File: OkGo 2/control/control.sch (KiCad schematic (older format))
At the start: 49 parts, among them P101 BATT, P102 BATT, P103 BATT_CASE, P104 KEYSW, P105 KEYSW, P110 SMA, SW101 LATCHING PUSH, SW102 KEYSWITCH, U101 FUSE 1A, U102 ADP3335, U103 BEZEL, U104 LCD_HD44780, U105 STM32F071CBT6, U106 RFM95W, U107 MEU1S0303ZC, U108 SWD, Y101 8MHz

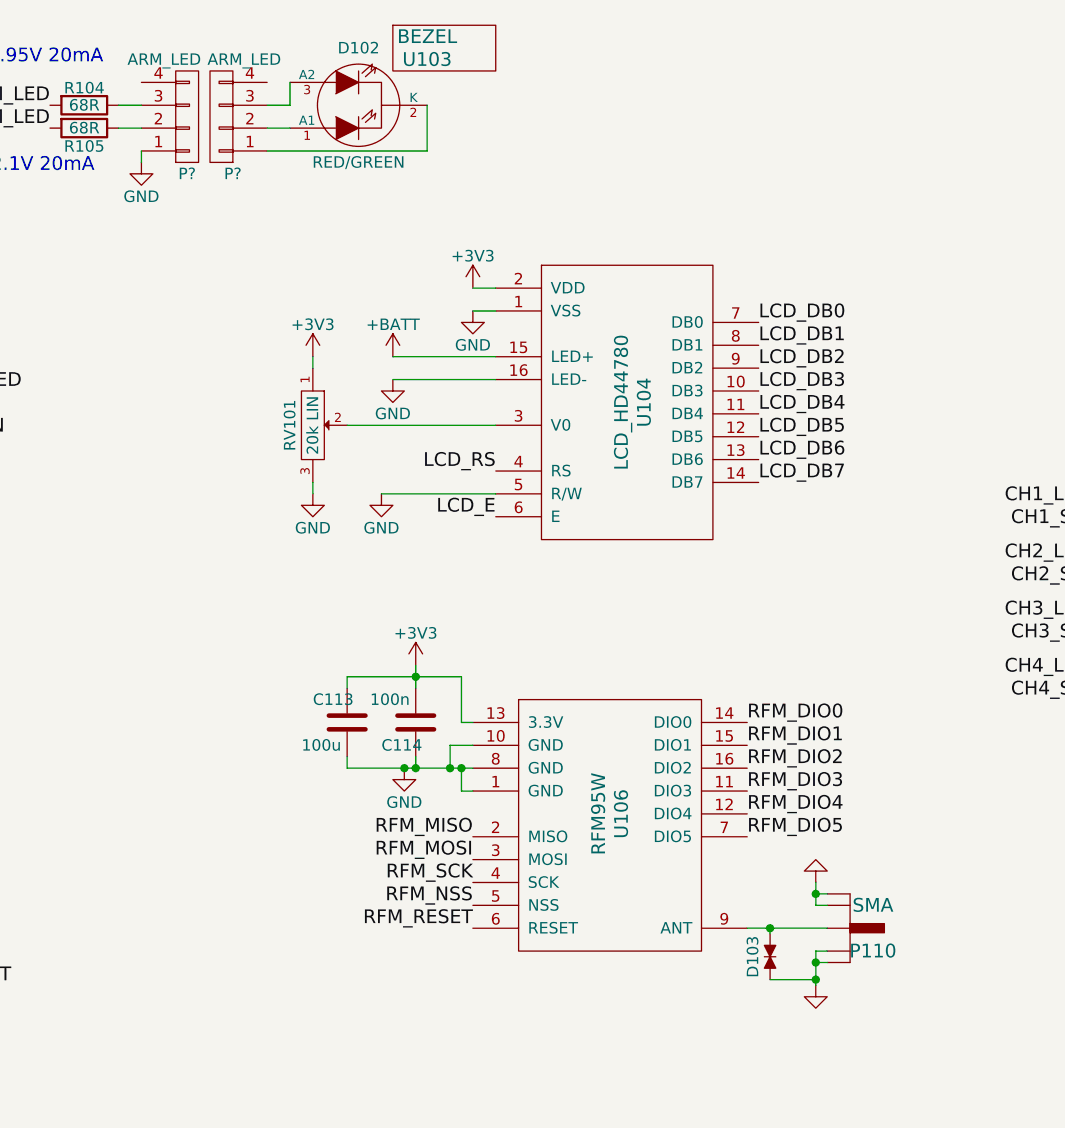
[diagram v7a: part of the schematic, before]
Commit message: Non-handsoldering footprints, fixes #17
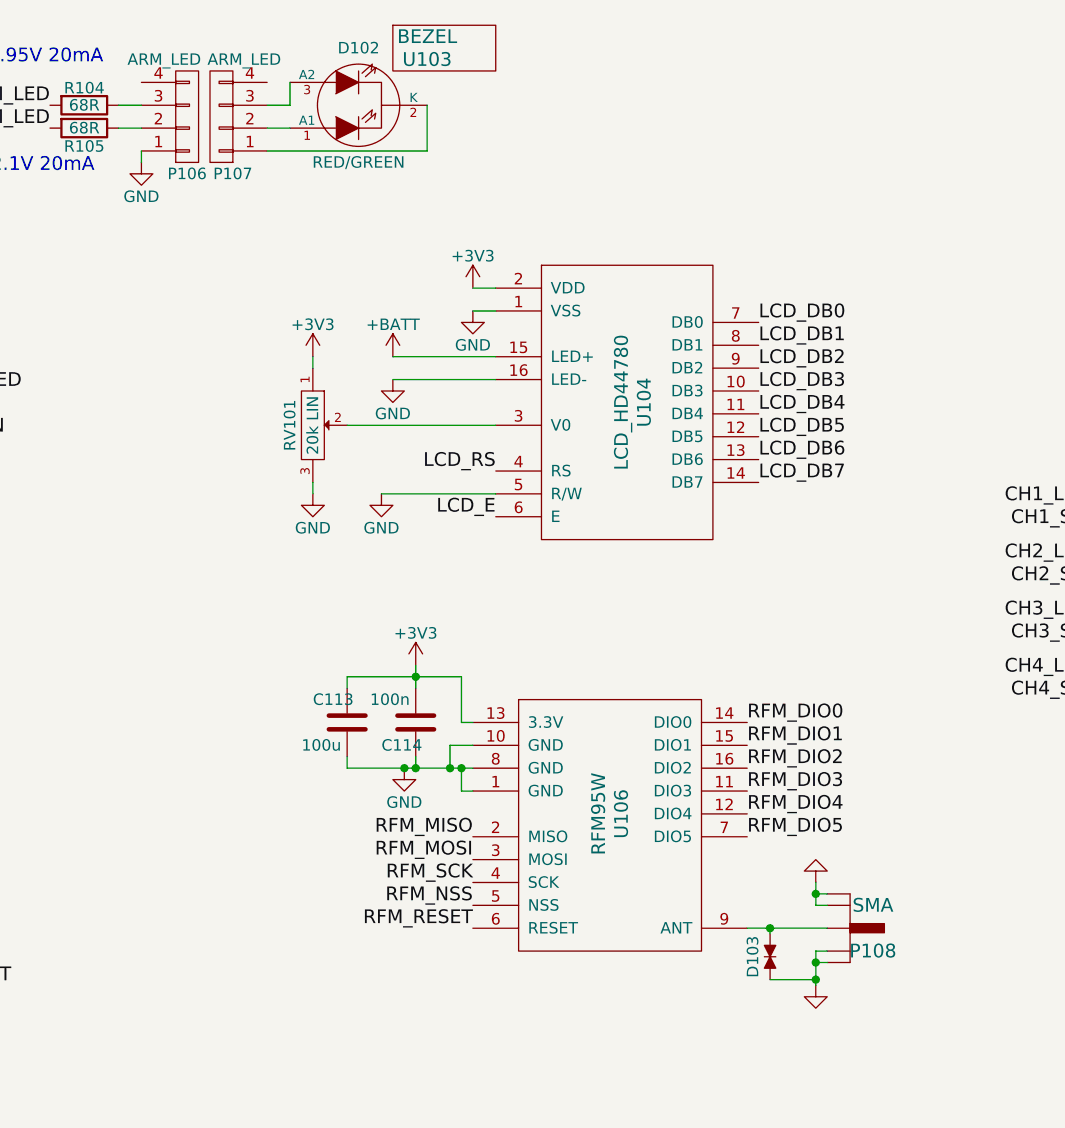
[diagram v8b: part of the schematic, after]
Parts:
- C101, C102, C103, C104, C105, C106, C107, C108, C109, C110, C111, C112, C114, R103: footprint Capacitors_SMD:C_0805_HandSoldering -> Capacitors_SMD:C_0805
- C113: footprint Capacitors_SMD:C_1206_HandSoldering -> Capacitors_SMD:C_1206
- D101, D103: footprint Resistors_SMD:R_0603_HandSoldering -> Resistors_SMD:R_0603
- R101, R102, R104, R105, R106: footprint Resistors_SMD:R_0805_HandSoldering -> Resistors_SMD:R_0805
- gave numbers to parts that had none: 2
- renumbered P110 to P108
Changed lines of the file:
@@
 F 0 "C102" H 8525 1400 50  0000 L CNN
 F 1 "2u2" H 8525 1200 50  0000 L CNN
-F 2 "Capacitors_SMD:C_0805_HandSoldering" H 8538 1150 30  0001 C CNN
+F 2 "Capacitors_SMD:C_0805" H 8538 1150 30  0001 C CNN
 F 3 "" H 8500 1300 60  0000 C CNN
 F 4 "2362106" H 8500 1300 60  0001 C CNN "Farnell"
@@
 F 0 "C101" H 10275 1350 50  0000 L CNN
 F 1 "2u2" H 10275 1150 50  0000 L CNN
-F 2 "Capacitors_SMD:C_0805_HandSoldering" H 10288 1100 30  0001 C CNN
+F 2 "Capacitors_SMD:C_0805" H 10288 1100 30  0001 C CNN
 F 3 "" H 10250 1250 60  0000 C CNN
 F 4 "2362106" H 10250 1250 60  0001 C CNN "Farnell"
@@
 F 0 "C110" V 1100 3975 50  0000 L CNN
 F 1 "1u" V 1100 3775 50  0000 L CNN
-F 2 "Capacitors_SMD:C_0805_HandSoldering" H 1088 3775 30  0001 C CNN
+F 2 "Capacitors_SMD:C_0805" H 1088 3775 30  0001 C CNN
 F 3 "" H 1050 3925 60  0000 C CNN
 F 4 "9227792" H 1050 3925 60  0001 C CNN "Farnell"
@@
 F 0 "C109" V 1100 3775 50  0000 L CNN
 F 1 "10n" V 1100 3525 50  0000 L CNN
-F 2 "Capacitors_SMD:C_0805_HandSoldering" H 1088 3575 30  0001 C CNN
+F 2 "Capacitors_SMD:C_0805" H 1088 3575 30  0001 C CNN
 F 3 "" H 1050 3725 60  0000 C CNN
 F 4 "2407341" H 1050 3725 60  0001 C CNN "Farnell"
@@
 F 0 "C108" V 1100 3575 50  0000 L CNN
 F 1 "4u7" V 1100 3325 50  0000 L CNN
-F 2 "Capacitors_SMD:C_0805_HandSoldering" H 1088 3375 30  0001 C CNN
+F 2 "Capacitors_SMD:C_0805" H 1088 3375 30  0001 C CNN
 F 3 "" H 1050 3525 60  0000 C CNN
 F 4 "1845742" H 1050 3525 60  0001 C CNN "Farnell"
@@
 F 0 "C107" H 3675 3425 50  0000 L CNN
 F 1 "100n" H 3675 3225 50  0000 L CNN
-F 2 "Capacitors_SMD:C_0805_HandSoldering" H 3688 3175 30  0001 C CNN
+F 2 "Capacitors_SMD:C_0805" H 3688 3175 30  0001 C CNN
 F 3 "" H 3650 3325 60  0000 C CNN
 F 4 "2407344" H 3650 3325 60  0001 C CNN "Farnell"
@@
 F 0 "R106" V 3800 4175 50  0000 C CNN
 F 1 "100R" V 3800 3925 50  0000 C CNN
-F 2 "Resistors_SMD:R_0805_HandSoldering" V 3630 4075 30  0001 C CNN
+F 2 "Resistors_SMD:R_0805" V 3630 4075 30  0001 C CNN
 F 3 "" H 3700 4075 30  0000 C CNN
 F 4 "2331783" H 3700 4075 60  0001 C CNN "Farnell"
@@
 F 0 "C111" H 4425 4475 50  0000 L CNN
 F 1 "15p" H 4425 4275 50  0000 L CNN
-F 2 "Capacitors_SMD:C_0805_HandSoldering" H 4438 4225 30  0001 C CNN
+F 2 "Capacitors_SMD:C_0805" H 4438 4225 30  0001 C CNN
 F 3 "" H 4400 4375 60  0000 C CNN
 F 4 "1414668" H 4400 4375 60  0001 C CNN "Farnell"
@@
 F 0 "C112" H 4625 4475 50  0000 L CNN
 F 1 "15p" H 4625 4275 50  0000 L CNN
-F 2 "Capacitors_SMD:C_0805_HandSoldering" H 4638 4225 30  0001 C CNN
+F 2 "Capacitors_SMD:C_0805" H 4638 4225 30  0001 C CNN
 F 3 "" H 4600 4375 60  0000 C CNN
 F 4 "1414668" H 4600 4375 60  0001 C CNN "Farnell"
@@
 F 0 "C105" V 1100 3175 50  0000 L CNN
 F 1 "4u7" V 1100 2925 50  0000 L CNN
-F 2 "Capacitors_SMD:C_0805_HandSoldering" H 1088 2975 30  0001 C CNN
+F 2 "Capacitors_SMD:C_0805" H 1088 2975 30  0001 C CNN
 F 3 "" H 1050 3125 60  0000 C CNN
 F 4 "1845742" H 1050 3125 60  0001 C CNN "Farnell"
@@
 F 0 "R101" V 7330 1100 50  0000 C CNN
 F 1 "3k3" V 7150 1100 50  0000 C CNN
-F 2 "Resistors_SMD:R_0805_HandSoldering" V 7180 1100 30  0001 C CNN
+F 2 "Resistors_SMD:R_0805" V 7180 1100 30  0001 C CNN
 F 3 "" H 7250 1100 30  0000 C CNN
 F 4 "9237682" H 7250 1100 60  0001 C CNN "Farnell"
@@
 F 0 "R103" V 7330 1500 50  0000 C CNN
 F 1 "10k" V 7150 1500 50  0000 C CNN
-F 2 "Capacitors_SMD:C_0805_HandSoldering" V 7180 1500 30  0001 C CNN
+F 2 "Capacitors_SMD:C_0805" V 7180 1500 30  0001 C CNN
 F 3 "" H 7250 1500 30  0000 C CNN
 F 4 "9237755" H 7250 1500 60  0001 C CNN "Farnell"
@@
 F 0 "D101" V 5800 950 50  0000 C CNN
 F 1 "TVS_small" H 5600 875 50  0001 C CNN
-F 2 "Resistors_SMD:R_0603_HandSoldering" H 5600 950 60  0001 C CNN
+F 2 "Resistors_SMD:R_0603" H 5600 950 60  0001 C CNN
 F 3 "" H 5600 950 60  0000 C CNN
 F 4 "2368174" H 5600 950 60  0001 C CNN "Farnell"
@@
 F 0 "D103" H 8800 6250 50  0000 C CNN
 F 1 "TVS_small" H 8800 6100 50  0001 C CNN
-F 2 "Resistors_SMD:R_0603_HandSoldering" H 8800 6175 60  0001 C CNN
+F 2 "Resistors_SMD:R_0603" H 8800 6175 60  0001 C CNN
 F 3 "" H 8800 6175 60  0000 C CNN
 F 4 "2368174" H 8800 6175 60  0001 C CNN "Farnell"
@@
 F 0 "C106" V 1000 3375 50  0000 L CNN
 F 1 "100n" V 1000 3075 50  0000 L CNN
-F 2 "Capacitors_SMD:C_0805_HandSoldering" H 1088 3175 30  0001 C CNN
+F 2 "Capacitors_SMD:C_0805" H 1088 3175 30  0001 C CNN
 F 3 "" H 1050 3325 60  0000 C CNN
 F 4 "2407344" H 1050 3325 60  0001 C CNN "Farnell"
@@
 F 0 "C104" V 1000 2975 50  0000 L CNN
 F 1 "100n" V 1000 2675 50  0000 L CNN
-F 2 "Capacitors_SMD:C_0805_HandSoldering" H 1088 2775 30  0001 C CNN
+F 2 "Capacitors_SMD:C_0805" H 1088 2775 30  0001 C CNN
 F 3 "" H 1050 2925 60  0000 C CNN
 F 4 "2407344" H 1050 2925 60  0001 C CNN "Farnell"
@@
 F 0 "C103" V 1000 2775 50  0000 L CNN
 F 1 "100n" V 1000 2475 50  0000 L CNN
-F 2 "Capacitors_SMD:C_0805_HandSoldering" H 1088 2575 30  0001 C CNN
+F 2 "Capacitors_SMD:C_0805" H 1088 2575 30  0001 C CNN
 F 3 "" H 1050 2725 60  0000 C CNN
 F 4 "2407344" H 1050 2725 60  0001 C CNN "Farnell"
@@
 F 0 "C114" H 7100 5250 50  0000 L CNN
 F 1 "100n" H 7050 5050 50  0000 L CNN
-F 2 "Capacitors_SMD:C_0805_HandSoldering" H 7288 5000 30  0001 C CNN
+F 2 "Capacitors_SMD:C_0805" H 7288 5000 30  0001 C CNN
 F 3 "" H 7250 5150 60  0000 C CNN
 F 4 "2407344" H 7250 5150 60  0001 C CNN "Farnell"
@@
 F 0 "C113" H 6800 5250 50  0000 L CNN
 F 1 "100u" H 6750 5050 50  0000 L CNN
-F 2 "Capacitors_SMD:C_1206_HandSoldering" H 6988 5000 30  0001 C CNN
+F 2 "Capacitors_SMD:C_1206" H 6988 5000 30  0001 C CNN
 F 3 "" H 6950 5150 60  0000 C CNN
 F 4 "2362115" H 6950 5150 60  0001 C CNN "Farnell"
@@
 $EndComp
 $Comp
-L SMA P110
+L SMA P108
 U 1 1 559E45E1
 P 9150 6050
-F 0 "P110" H 9250 5950 60  0000 C CNN
+F 0 "P108" H 9250 5950 60  0000 C CNN
 F 1 "SMA" H 9250 6150 60  0000 C CNN
 F 2 "common:SMA-142-0701-801" H 9150 6050 60  0001 C CNN
@@
 F 0 "R102" V 2130 1200 50  0000 C CNN
 F 1 "10k" V 2050 1200 50  0000 C CNN
-F 2 "Resistors_SMD:R_0805_HandSoldering" V 1980 1200 30  0001 C CNN
+F 2 "Resistors_SMD:R_0805" V 1980 1200 30  0001 C CNN
 F 3 "" H 2050 1200 30  0000 C CNN
 F 4 "2331808" H 2050 1200 60  0001 C CNN "Farnell"
@@
 F 0 "R104" V 5725 2450 50  0000 C CNN
 F 1 "68R" V 5800 2450 50  0000 C CNN
-F 2 "Resistors_SMD:R_0805_HandSoldering" V 5730 2450 30  0001 C CNN
+F 2 "Resistors_SMD:R_0805" V 5730 2450 30  0001 C CNN
 F 3 "" H 5800 2450 30  0000 C CNN
 F 4 "2332055" H 5800 2450 60  0001 C CNN "Farnell"
@@
 F 0 "R105" V 5880 2550 50  0000 C CNN
 F 1 "68R" V 5800 2550 50  0000 C CNN
-F 2 "Resistors_SMD:R_0805_HandSoldering" V 5730 2550 30  0001 C CNN
+F 2 "Resistors_SMD:R_0805" V 5730 2550 30  0001 C CNN
 F 3 "" H 5800 2550 30  0000 C CNN
 F 4 "2332055" H 5800 2550 60  0001 C CNN "Farnell"
@@
 	7300 2650 6600 2650
 $Comp
-L CONN_01X04 P?
+L CONN_01X04 P107
 U 1 1 55AB5A44
 P 6400 2500
-F 0 "P?" H 6350 2750 50  0000 C CNN
+F 0 "P107" H 6350 2750 50  0000 C CNN
 F 1 "ARM_LED" H 6300 2250 50  0000 C CNN
 F 2 "" H 6400 2500 60  0000 C CNN
@@
 $EndComp
 $Comp
-L CONN_01X04 P?
+L CONN_01X04 P106
 U 1 1 55AB5EAE
 P 6250 2500
-F 0 "P?" H 6250 2750 50  0000 C CNN
+F 0 "P106" H 6250 2750 50  0000 C CNN
 F 1 "ARM_LED" H 6150 2250 50  0000 C CNN
 F 2 "common:JST-PA-4" H 6250 2500 60  0001 C CNN
